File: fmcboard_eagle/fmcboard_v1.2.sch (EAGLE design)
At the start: 88 parts, among them IC1 OPA699ID, IC10 LTC6229IMS8E#TRPBF, IC11 LTC6229IMS8E#TRPBF, IC2 LM2662M_NOPB, IC3 LTC6229IMS8E#TRPBF, IC4 LTC6229IMS8E#TRPBF, IC5 LM358, IC6 OPA699ID, IC7 OPA699ID, IC8 LTC6229IMS8E#TRPBF, IC9 LTC6229IMS8E#TRPBF, J1 8pin, J12 4p-2.54, J2 ASP-134604-01, J3 4p-2.54, J4 4p-2.54, J5 8pin, U1 TXS0108EPWR

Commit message: Before routing
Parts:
- removed R1, R12: 20k, resistor:R-TRIMM3296W
- added J6, J7: 4p-2.54, Seeed-Connector:DIP-BLACK-FEMALE-HEADER-VERT(4P-2.54)
- added R49: 50, SparkFun-Resistors:RESISTORAXIAL-0.3
- added R_O1, R_O2: 20k, resistor:R-TRIMM3296W
- renumbered R7 to R_VH, R8 to R_VL
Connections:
- new net TRANSIN: IC4.-INA, R11.2, R49.1
- net GND: now also J1.1, J1.2, J1.7, J1.8
- net IO1: now also R49.2; no longer IC4.-INA, R11.2
- net N$2: now also R_O2.S; no longer R12.S
- net N$8: now also R_O1.S; no longer R1.S
- net VS+: now also J6.P$1, J6.P$2, J6.P$3, J6.P$4, R_O1.E, R_O2.E; no longer R1.E, R12.E
- net VS-: now also J7.P$1, J7.P$2, J7.P$3, J7.P$4, R_O1.A, R_O2.A; no longer R1.A, R12.A
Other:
- note added: "Since the input goes to a virtual GND at the op amp, need 50 Ohm? Should use _one_ of the 50 Ohm resistors here - I believe the series one."

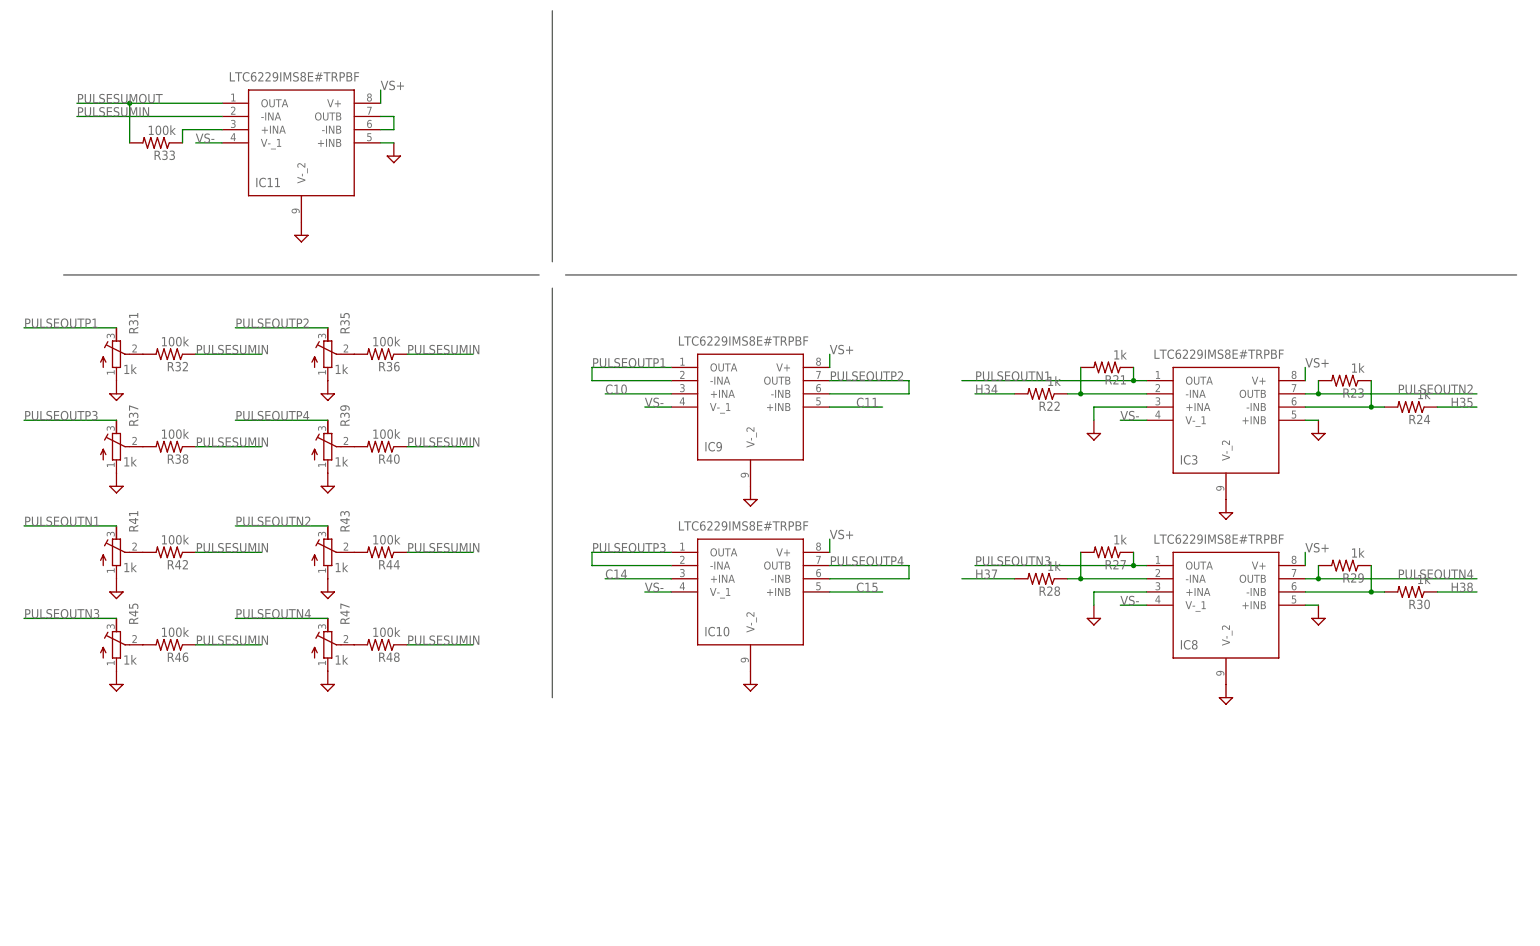
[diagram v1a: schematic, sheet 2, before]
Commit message: v1.21 make exposed pads VS- not GND, divide voltage before op amp buffers, add op amp decoupling caps, improve layout
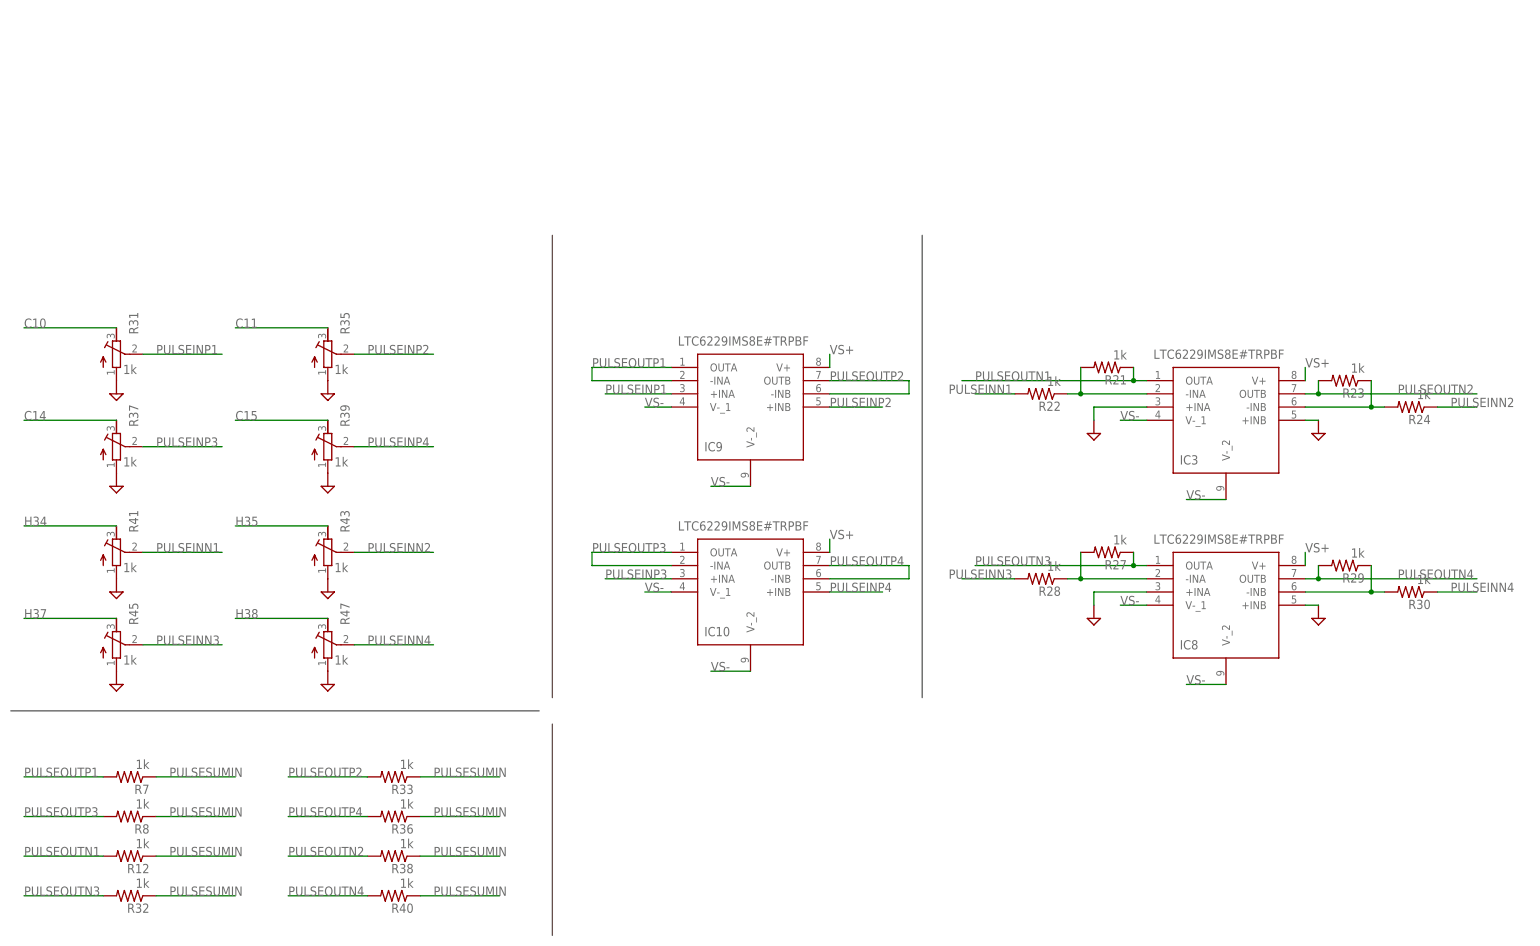
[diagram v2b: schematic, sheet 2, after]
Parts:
- removed IC11: LTC6229IMS8E#TRPBF, LTC6229IMS8E#TRPBF:LTC6229IMS8E#TRPBF
- removed R42, R44, R46, R48: 100k, rcl:R-US_R0805
- added C15, C16, C17, C18, C19, C20, C21, C22, C23, C24, C25, C26, C27, C28, C29, C30, C31, C6: 0.1uF, SparkFun-Passives:CAP0805
- added R1, R12, R7, R8: 1k, rcl:R-US_R0805
- C1: value 10uF -> 47uF
- R32, R33, R36, R38, R40: value 100k -> 1k
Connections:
- removed net N$15: R31.S, R32.2
- removed net N$16: IC11.-INB, IC11.OUTB
- removed net N$17: IC11.+INA, R33.1
- removed net N$19: R35.S, R36.2
- removed net N$20: R37.S, R38.2
- removed net N$21: R39.S, R40.2
- removed net N$22: R41.S, R42.2
- removed net N$23: R43.S, R44.2
- removed net N$24: R45.S, R46.2
- removed net N$25: R47.S, R48.2
- removed net N$7: IC4.-INB, IC4.OUTB
- new net N$27: IC4.+INB, R1.1
- new net PULSEINN1: R22.2, R41.S
- new net PULSEINN2: R24.1, R43.S
- new net PULSEINN3: R28.2, R45.S
- new net PULSEINN4: R30.1, R47.S
- new net PULSEINP1: IC9.+INA, R31.S
- new net PULSEINP2: IC9.+INB, R35.S
- new net PULSEINP3: IC10.+INA, R37.S
- new net PULSEINP4: IC10.+INB, R39.S
- net C10: now also R31.E; no longer IC9.+INA
- net C11: now also R35.E; no longer IC9.+INB
- net C14: now also R37.E; no longer IC10.+INA
- net C15: now also R39.E; no longer IC10.+INB
- net GND: now also C15.2, C16.2, C17.2, C18.2, C19.2, C20.2, C21.2, C22.2, C23.2, C24.2, C25.2, C26.2, C27.2, C28.2, C29.2, C30.2, C31.2, C6.2; no longer IC10.V-_2, IC11.+INB, IC11.V-_2, IC3.V-_2, IC4.+INB, IC4.V-_2, IC8.V-_2, IC9.V-_2
- net H34: now also R41.E; no longer R22.2
- net H35: now also R43.E; no longer R24.1
- net H37: now also R45.E; no longer R28.2
- net H38: now also R47.E; no longer R30.1
- net PULSEOUTN1: now also R12.2; no longer R41.E
- net PULSEOUTN2: now also R38.2; no longer R43.E
- net PULSEOUTN3: now also R32.2; no longer R45.E
- net PULSEOUTN4: now also R40.2; no longer R47.E
- net PULSEOUTP1: now also R7.2; no longer R31.E
- net PULSEOUTP2: now also R33.2; no longer R35.E
- net PULSEOUTP3: now also R8.2; no longer R37.E
- net PULSEOUTP4: now also R36.2; no longer R39.E
- net PULSESUMIN: now also IC4.-INB, R12.1, R33.1, R7.1, R8.1; no longer IC11.-INA, R42.1, R44.1, R46.1, R48.1
- net PULSESUMOUT: now also IC4.OUTB, R1.2; no longer IC11.OUTA, R33.2
- net VS+: now also C16.1, C18.1, C20.1, C22.1, C24.1, C26.1, C28.1, C30.1, C6.1; no longer IC11.V+
- net VS-: now also C15.1, C17.1, C19.1, C21.1, C23.1, C25.1, C27.1, C29.1, C31.1, IC10.V-_2, IC3.V-_2, IC4.V-_2, IC8.V-_2, IC9.V-_2; no longer IC11.V-_1
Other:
- note added: "Decoupling"
- note added: "Input goes to a virtual GND at the op amp, so need 50 Ohm? Use _one_ of the 50 Ohm resistors here (?)"
- note added: "Negative output inverting buffers"
- note added: "Positive output buffers"
- note added: "Pulse resistors for summing"
- note added: "Pulse voltage dividers"
- note removed: "Negative output pulses"
- note removed: "Positive output pulses"
- note removed: "Since the input goes to a virtual GND at the op amp, need 50 Ohm? Should use _one_ of the 50 Ohm resistors here - I believe the series one."
- moved on the sheet: IC4, OPIN, R11, R2, R32, R33, R36, R38, R40, R49

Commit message: Fixes for v1.21, amps etc
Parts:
- removed R49: 50, SparkFun-Resistors:RESISTORAXIAL-0.3
- added C32, C34, C35, C36, C37: 5pF, SparkFun-Passives:CAP0805
- added C33: 2pF, SparkFun-Passives:CAP0805
- R11: value 33k -> 5k
- R2: device SparkFun-Resistors:RESISTORAXIAL-0.3 -> rcl:R-US_R0805
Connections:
- removed net N$27: IC4.+INB, R1.1
- net GND: now also IC4.+INB; no longer R2.1
- net IO1: no longer R49.2
- net N$12: now also C35.2
- net N$13: now also C34.2
- net N$14: now also C37.1
- net N$4: now also C36.1
- net PULSEINN1: now also C34.1
- net PULSEINN2: now also C36.2
- net PULSEINN3: now also C35.1
- net PULSEINN4: now also C37.2
- net PULSESUMIN: now also C32.1, R1.1
- net PULSESUMOUT: now also C32.2
- net TRANSIN: now also C33.1, R2.1; no longer R49.1
- net TRANSOUT: now also C33.2
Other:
- note removed: "Input goes to a virtual GND at the op amp, so need 50 Ohm? Use _one_ of the 50 Ohm resistors here (?)"
- moved on the sheet: OPIN, R2

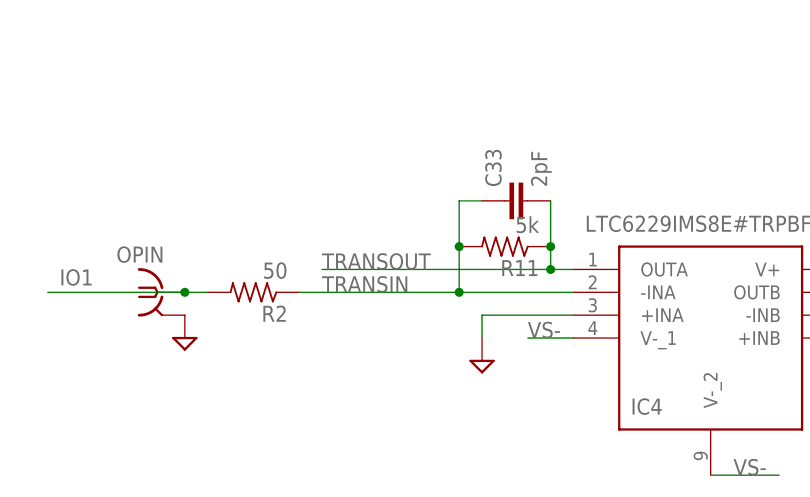
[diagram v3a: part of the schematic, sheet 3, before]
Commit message: Tune the trans amp gain and compensation
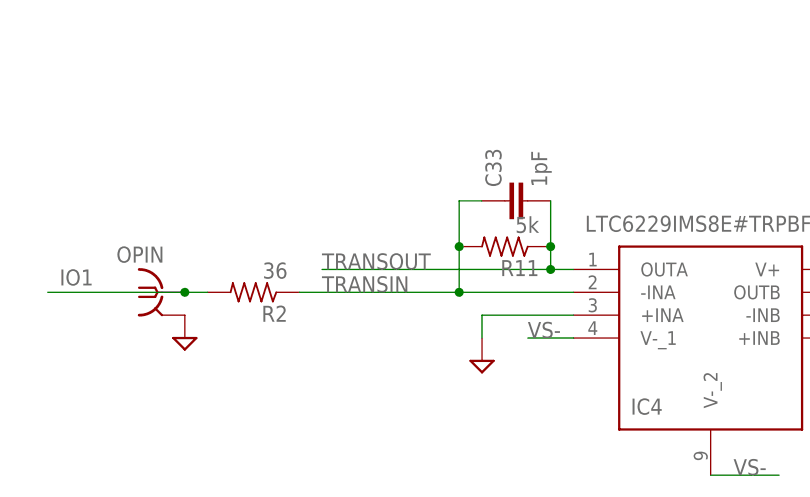
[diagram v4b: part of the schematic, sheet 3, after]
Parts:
- C33: value 2pF -> 1pF
- R2: value 50 -> 36
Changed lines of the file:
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@@
 <part name="R40" library="rcl" library_urn="urn:adsk.eagle:library:334" deviceset="R-US_" device="R0805" package3d_urn="urn:adsk.eagle:package:23553/2" value="1k"/>
 <part name="SUPPLY25" library="supply2" library_urn="urn:adsk.eagle:library:372" deviceset="GND" device=""/>
-<part name="R2" library="rcl" library_urn="urn:adsk.eagle:library:334" deviceset="R-US_" device="R0805" package3d_urn="urn:adsk.eagle:package:23553/2" value="50"/>
+<part name="R2" library="rcl" library_urn="urn:adsk.eagle:library:334" deviceset="R-US_" device="R0805" package3d_urn="urn:adsk.eagle:package:23553/2" value="36"/>
 <part name="C34" library="SparkFun-Passives" deviceset="CAP" device="0805" value="5pF"/>
 <part name="C35" library="SparkFun-Passives" deviceset="CAP" device="0805" value="5pF"/>
@@
 <part name="C37" library="SparkFun-Passives" deviceset="CAP" device="0805" value="5pF"/>
 <part name="C32" library="SparkFun-Passives" deviceset="CAP" device="0805" value="5pF"/>
-<part name="C33" library="SparkFun-Passives" deviceset="CAP" device="0805" value="2pF"/>
+<part name="C33" library="SparkFun-Passives" deviceset="CAP" device="0805" value="1pF"/>
 </parts>
 <sheets>

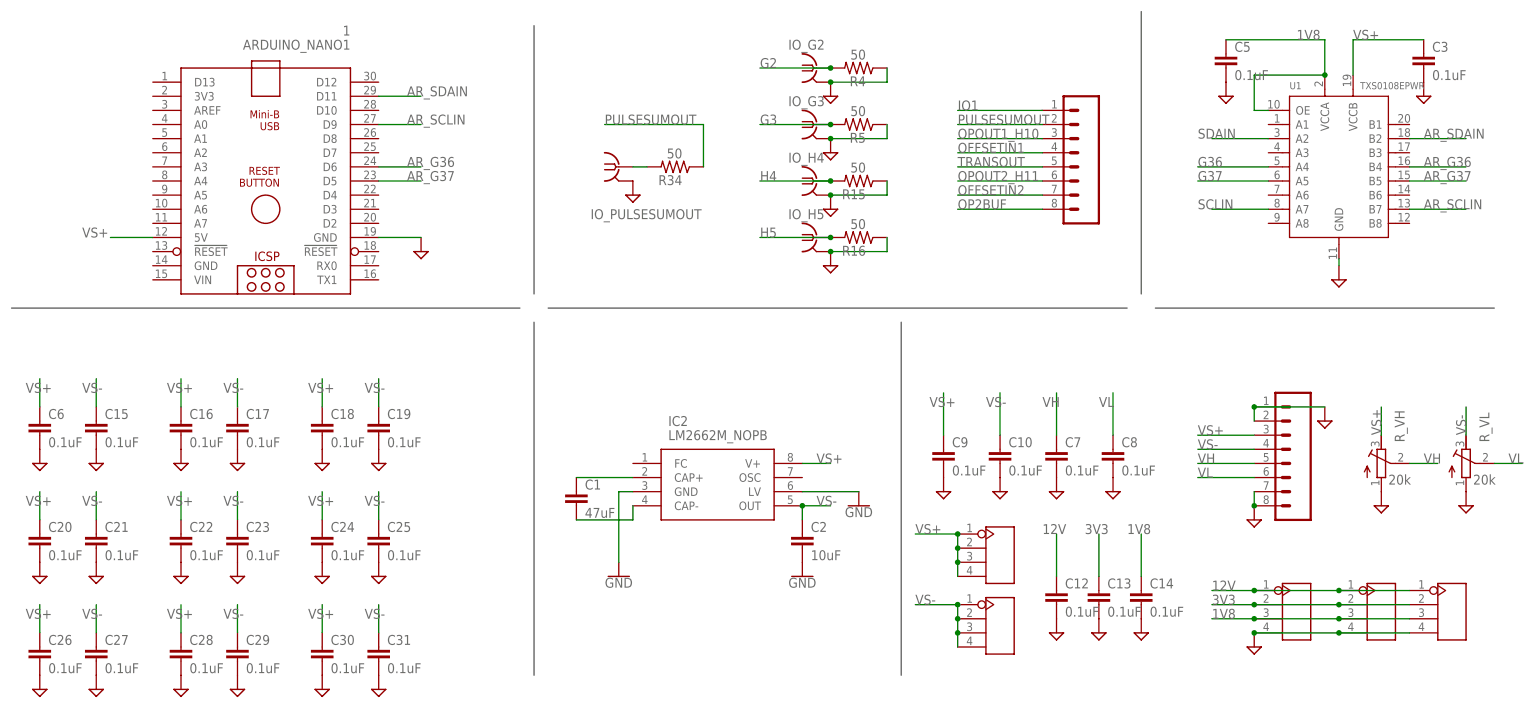
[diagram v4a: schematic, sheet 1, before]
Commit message: cleaned up a bit, added topgnd cutouts still need to fix power, layout of amp feedback, and route
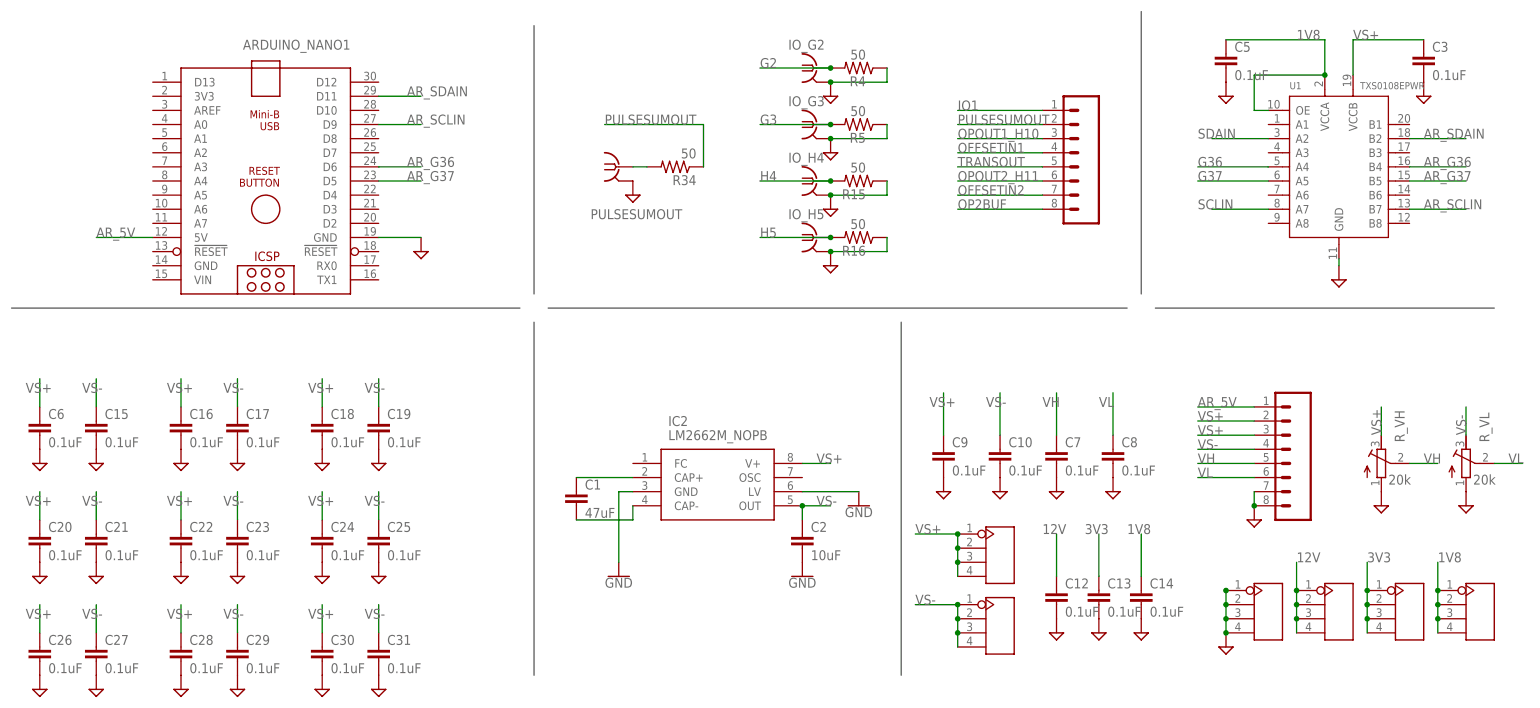
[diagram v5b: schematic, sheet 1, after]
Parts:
- added J8: 4p-2.54, Seeed-Connector:DIP-BLACK-FEMALE-HEADER-VERT(4P-2.54)
- added R42: 50, rcl:R-US_R0805
- C32, C34, C35, C36, C37: value 5pF -> 1pF
- R2: value 36 -> 50
- R34: device SparkFun-Resistors:RESISTORAXIAL-0.3 -> rcl:R-US_R0805
- renumbered IO_PULSESUMOUT to PULSESUMOUT
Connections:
- new net AR_5V: ARDUINO_NANO1.5V, J1.1
- net 12V: now also J8.P$1, J8.P$2, J8.P$3, J8.P$4; no longer J12.P$1, J3.P$1, J4.P$1
- net 1V8: now also J12.P$1, J12.P$2, J12.P$4; no longer J3.P$3, J4.P$3
- net 3V3: now also J3.P$1, J3.P$3, J3.P$4; no longer J12.P$2, J4.P$2
- net GND: now also J4.P$1, J4.P$2, J4.P$3, R42.2; no longer J1.1, J1.2, J12.P$4, J3.P$4
- net IO1: now also R42.1
- net VS+: now also J1.2; no longer ARDUINO_NANO1.5V
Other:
- note added: "Can use jumper to connect AR_5V and VS+"
- moved on the sheet: OPIN

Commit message: did power still need to fix layout of amp feedback, and route
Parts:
- removed IC2: LM2662M_NOPB, LM2662M_NOPB:LM2662M_NOPB
- added C38, C39, C40, C41: 10uF, SparkFun-Capacitors:CAPPTH1
- added C42, C43, C44, C45, C46, C47: 0.1uF, SparkFun-Passives:CAP0805
- added IC11: 7805TV, linear:7805TV
- added IC12: 7905, linear:7905T
- added L1, L2: 10uH, rcl:L-US6000-XXX-RC
- C1: value 47uF -> 10uF
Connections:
- new net VIN+: C39.1, C42.1, J1.5, L1.1
- new net VIN-: C40.1, C44.2, J1.7, L2.1
- net GND: now also C1.2, C2.1, C38.2, C39.2, C40.2, C41.2, C42.2, C43.2, C44.1, C45.1, C46.1, C47.2, IC11.GND, IC12.GND, J1.6; no longer C2.2, IC2.GND, IC2.LV, J1.7
- net N$5: now also C38.1, C43.1, IC11.VI, L1.2; no longer C1.1, IC2.CAP+
- net N$6: now also C41.1, C45.2, IC12.VI, L2.2; no longer C1.2, IC2.CAP-
- net VH: now also J1.3; no longer J1.5
- net VL: now also J1.4; no longer J1.6
- net VS+: now also C1.1, C47.1, IC11.VO; no longer IC2.V+, J1.3
- net VS-: now also C2.2, C46.2, IC12.VO; no longer C2.1, IC2.OUT, J1.4
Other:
- note added: "Linear +- power supplies and smoothing"
- note removed: "Negative V supply"

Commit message: did power still need to fix layout of amp feedback, and route
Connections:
- net N$5 renamed VIN+CLEAN
- net N$6 renamed VIN-CLEAN
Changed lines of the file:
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@@
 </segment>
 </net>
-<net name="N$5" class="0">
+<net name="VIN+CLEAN" class="0">
 <segment>
 <pinref part="IC11" gate="A1" pin="VI"/>
@@
 <wire x1="20.32" y1="38.1" x2="25.4" y2="38.1" width="0.1524" layer="91"/>
 <pinref part="C43" gate="G$1" pin="1"/>
+<label x="17.78" y="35.56" size="1.778" layer="95"/>
 </segment>
 </net>
-<net name="N$6" class="0">
+<net name="VIN-CLEAN" class="0">
 <segment>
 <pinref part="IC12" gate="A1" pin="VI"/>
@@
 <wire x1="20.32" y1="12.7" x2="25.4" y2="12.7" width="0.1524" layer="91"/>
 <pinref part="C45" gate="G$1" pin="2"/>
+<label x="17.78" y="10.16" size="1.778" layer="95"/>
 </segment>
 </net>
